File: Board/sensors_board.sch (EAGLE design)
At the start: 7 parts, among them U1 TEM-HUM-AM2302(4P-25.0X15.0MM)

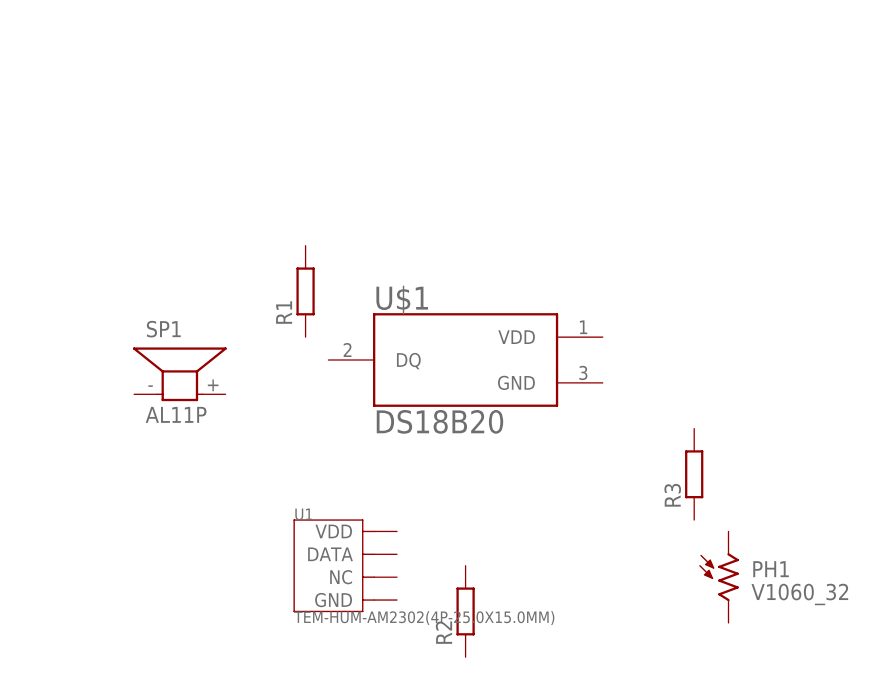
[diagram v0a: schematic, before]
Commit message: Add new files
- motherboard scheme
- ATtiny13 code
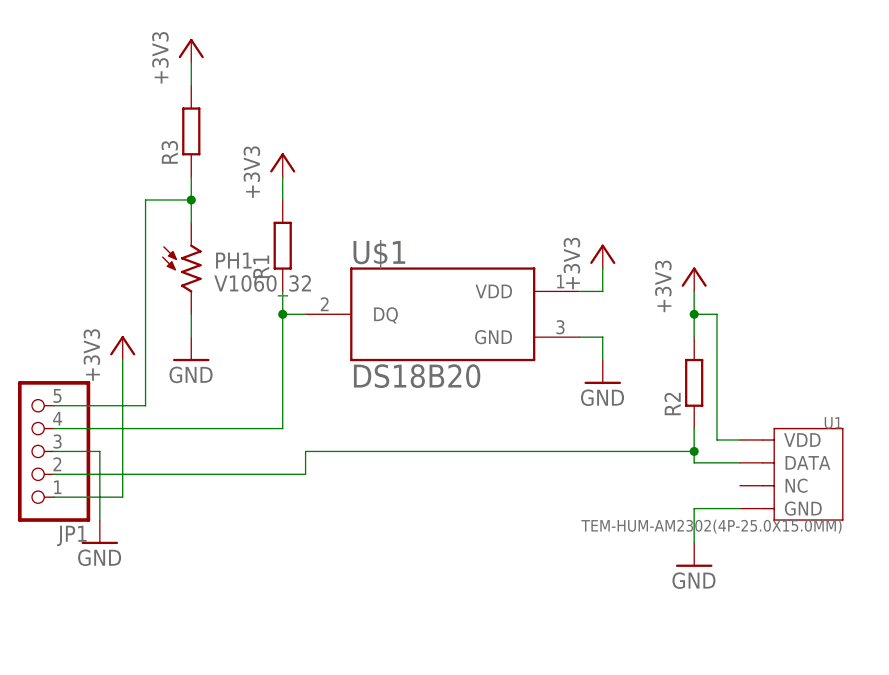
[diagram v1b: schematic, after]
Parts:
- removed SP1: AL11P, buzzer:AL11P
- added JP1: (no value), pinhead:PINHD-1X5/90
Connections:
- new net +3V3: JP1.1, R1.2, R2.2, R3.2, U$1.VDD, U1.VDD
- new net GND: JP1.3, PH1.2, U$1.GND, U1.GND
- new net N$1: JP1.2, R2.1, U1.DATA
- new net N$2: JP1.4, R1.1, U$1.DQ
- new net N$3: JP1.5, PH1.1, R3.1
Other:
- moved on the sheet: PH1, R1, R2, R3, U$1, U1
